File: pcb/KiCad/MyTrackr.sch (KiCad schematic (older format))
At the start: 40 parts, among them CN1 GPS_ANTENNA, CON1 MICRO_SD, J1 REGULATOR_3V3, J2 CONN_ICSP, J3 CONN_SERIAL, J4 CONN_BAT, P1 CONN_OLED, Q1 Q_PMOS_GSD, SW1 BTN_RESET, SW2 BTN_SEL, SW3 BTN_NEXT, SW4 BTN_PREV, SW5 BTN_BACK, U1 ATMEGA328PA, U2 GPS-NEO-6M, U3 24AA32

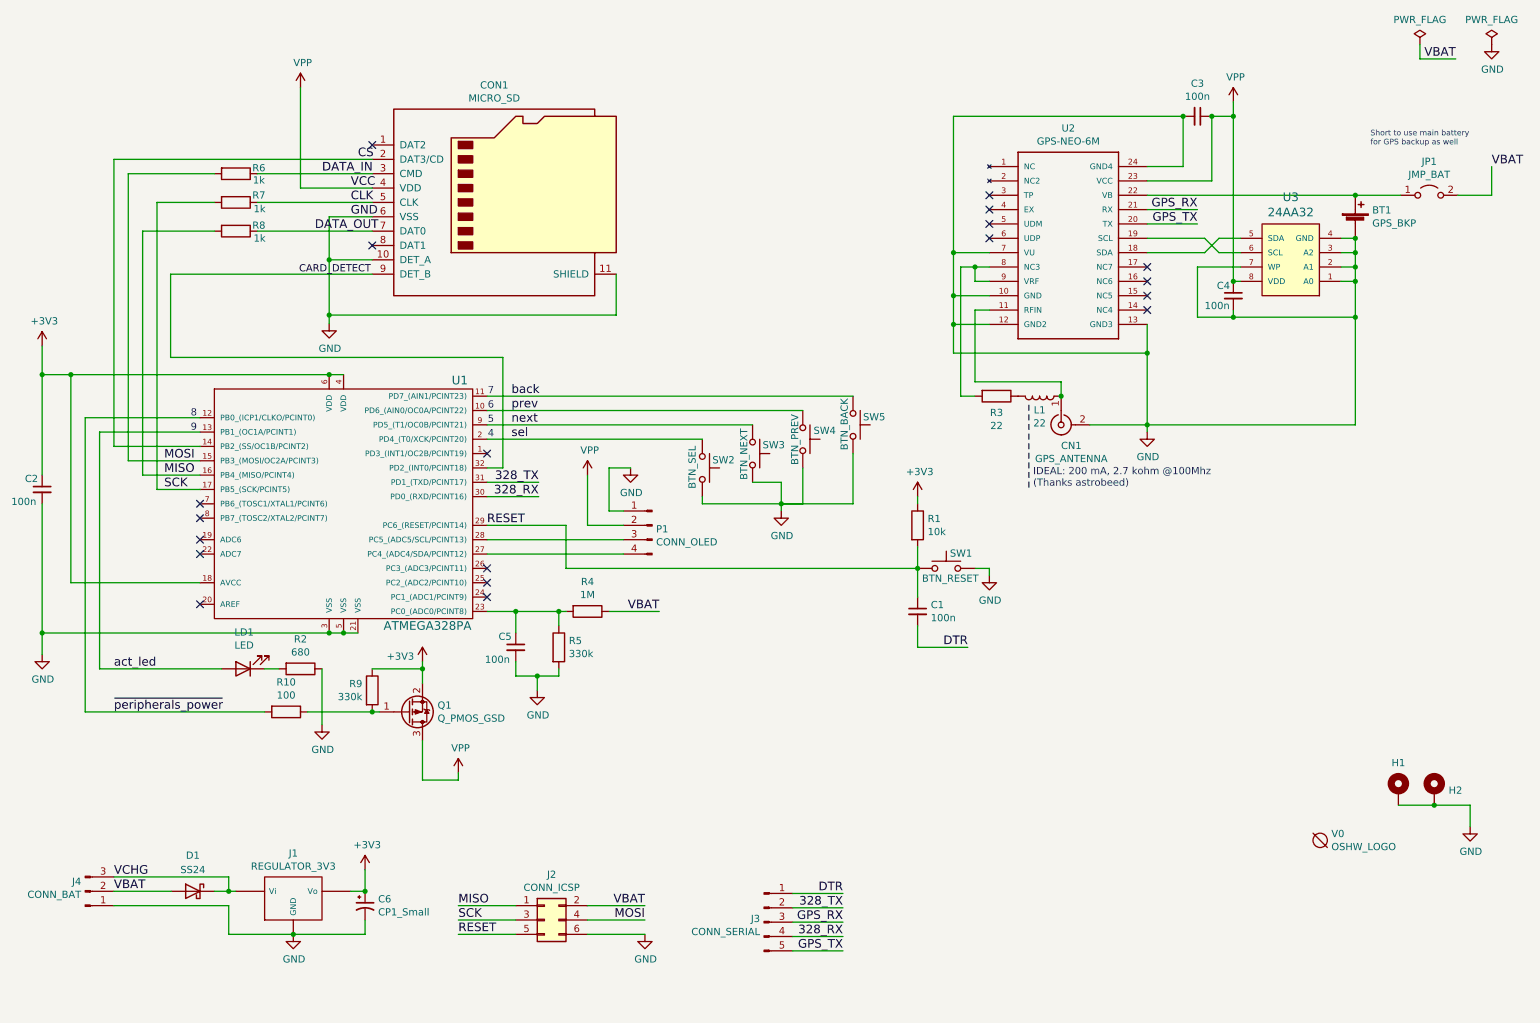
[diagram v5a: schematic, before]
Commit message: Use KiCad's 328 symbol and add MOSFET-bypass jumper
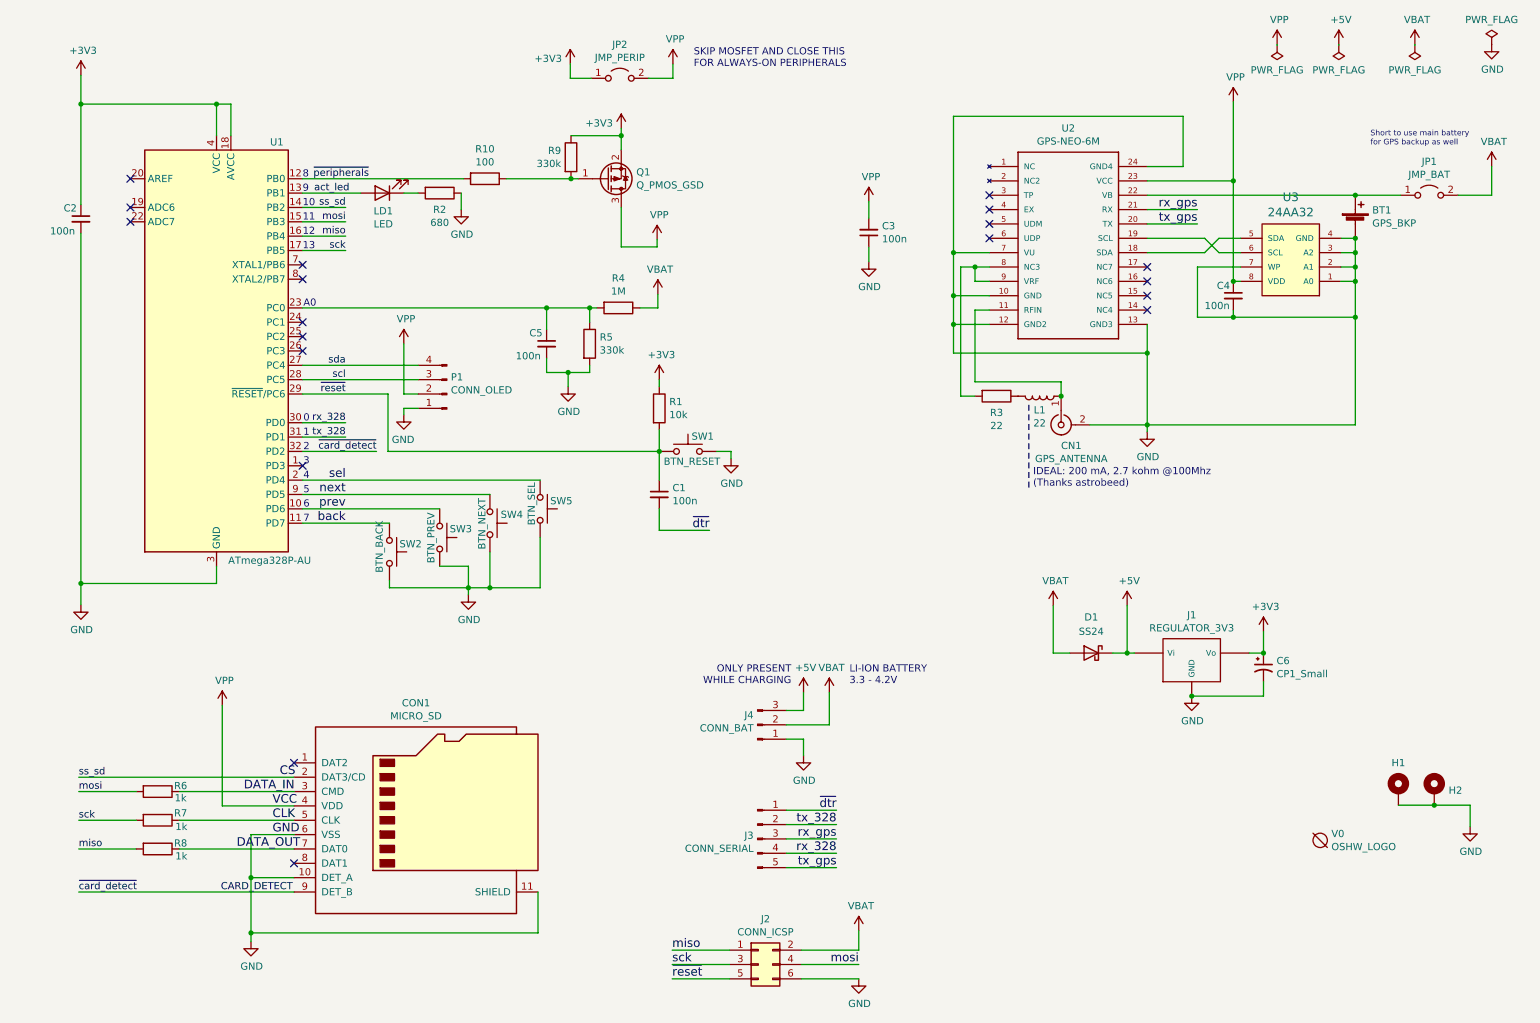
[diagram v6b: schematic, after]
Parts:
- removed U1: ATMEGA328PA, Package_QFP:TQFP-32_7x7mm_P0.8mm, symbol atmega328:ATMEGA48_88_168_328P-32SMD
- added JP2: JMP_PERIP, Jumper:SolderJumper-2_P1.3mm_Open_TrianglePad1.0x1.5mm, symbol Jumper:Jumper_2_Open
- added U1: ATmega328P-AU, Package_QFP:TQFP-32_7x7mm_P0.8mm, symbol MCU_Microchip_ATmega:ATmega328P-AU
- SW2: value BTN_SEL -> BTN_BACK
- SW3: value BTN_NEXT -> BTN_PREV
- SW4: value BTN_PREV -> BTN_NEXT
- SW5: value BTN_BACK -> BTN_SEL
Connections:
- net +3V3: now also JP2.1 (A), U1.18 (AVCC), U1.4 (VCC), U1.6 (VCC)
- net CARD_DETECT: now also U1.32 (PD2)
- net CS: now also U1.14 (PB2)
- net GND: now also C3.1, U1.21 (GND), U1.3 (GND), U1.5 (GND); no longer C3.2
- net VPP: now also C3.2, JP2.2 (B); no longer C3.1
- net act_led: now also U1.13 (PB1)
- net back: now also SW2.1, U1.11 (PD7); no longer SW5.1
- net next: now also SW4.1, U1.9 (PD5); no longer SW3.1
- net prev: now also SW3.1, U1.10 (PD6); no longer SW4.1
- net sel: now also SW5.1, U1.2 (PD4); no longer SW2.1
- net at C5.1, R4.2, R5.1: now also U1.23 (PC0)
- net scl: now reaches P1.3 (Pin_3)
- net scl: now also U1.28 (PC5)
- net sda: now reaches P1.4 (Pin_4)
- net sda: now also U1.27 (PC4)
- net 328_RX renamed rx_328
- net rx_328: now also U1.30 (PD0)
- net 328_TX renamed tx_328
- net tx_328: now also U1.31 (PD1)
- net DTR renamed ~dtr
- net GPS_RX renamed rx_gps
- net GPS_TX renamed tx_gps
- net MISO renamed miso
- net miso: now also U1.16 (PB4)
- net MOSI renamed mosi
- net mosi: now also U1.15 (PB3)
- net RESET renamed ~reset
- net ~reset: now also U1.29 (~RESET~/PC6)
- net SCK renamed sck
- net sck: now also U1.17 (PB5)
- net VCHG renamed +5V
- net ~peripherals_power renamed ~peripherals
- net ~peripherals: now also U1.12 (PB0)
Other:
- note added: "0"
- note added: "1"
- note added: "10"
- note added: "11"
- note added: "12"
- note added: "13"
- note added: "2"
- note added: "3"
- note added: "A0"
- note added: "LI-ION BATTERY\n3.3 - 4.2V"
- note added: "ONLY PRESENT\nWHILE CHARGING"
- note added: "SKIP MOSFET AND CLOSE THIS\nFOR ALWAYS-ON PERIPHERALS"
- moved on the sheet: C1, C2, C3, C5, C6, CON1, D1, J1, J2, J3, J4, LD1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

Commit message: Make custom footprint for reset button
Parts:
- SW1: footprint Button_Switch_SMD:SW_SPST_REED_CT05-XXXX-J1 -> MyTrackr:SingleButtonSmall
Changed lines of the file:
@@
 F 0 "SW1" H 5530 3740 50  0000 R CNN
 F 1 "BTN_RESET" H 5575 3565 50  0000 R CNN
-F 2 "Button_Switch_SMD:SW_SPST_REED_CT05-XXXX-J1" H 5350 3835 50  0001 C CNN
+F 2 "MyTrackr:SingleButtonSmall" H 5350 3835 50  0001 C CNN
 F 3 "~" H 5350 3835 50  0001 C CNN
 	1    5350 3635
